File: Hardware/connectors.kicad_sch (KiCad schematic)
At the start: 0 parts

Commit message: Finalize schematic: Add connectors, LEDs, Buzzer and fix all ERC errors
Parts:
- added D1: D_Schottky, symbol Device:D_Schottky
- added J1: USB_C_Receptacle_USB2.0_16P, symbol Connector:USB_C_Receptacle_USB2.0_16P
- added J10: RX1, symbol Connector_Generic:Conn_01x01
- added J11: TX1, symbol Connector_Generic:Conn_01x01
- added J12, J16, J21, J25, J29, J3, J8: GND, symbol Connector_Generic:Conn_01x01
- added J13, J20, J22, J26, J30, J4, J6, J9: +5V, symbol Connector_Generic:Conn_01x01
- added J14: CAM_VIDEO_IN, symbol Connector_Generic:Conn_01x01
- added J15: +9V, symbol Connector_Generic:Conn_01x01
- added J17: VTX_VIDEO_OUT, symbol Connector_Generic:Conn_01x01
- added J18: TX3, symbol Connector_Generic:Conn_01x01
- added J19: RX3, symbol Connector_Generic:Conn_01x01
- added J2: Conn_01x08, symbol Connector_Generic:Conn_01x08
- added J23: RX2, symbol Connector_Generic:Conn_01x01
- added J24: TX2, symbol Connector_Generic:Conn_01x01
- added J27: RX5, symbol Connector_Generic:Conn_01x01
- added J28: TX5, symbol Connector_Generic:Conn_01x01
- added J31: RX6, symbol Connector_Generic:Conn_01x01
- added J32: TX6, symbol Connector_Generic:Conn_01x01
- added J5: LED_STRIP, symbol Connector_Generic:Conn_01x01
- added J7: BUZZER-, symbol Connector_Generic:Conn_01x01
- added R10, R9: 5.1k, symbol Device:R
- added R15: 330Ω, symbol Device:R
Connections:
- new net: D1.2 (A), J1.A4 (VBUS), J1.A9 (VBUS), J1.B4 (VBUS), J1.B9 (VBUS)
- new net: J1.A5 (CC1), R9.1
- new net: J1.B5 (CC2), R10.1
- new net: J5.1 (Pin_1), R15.2
- new net +5V: D1.1 (K), J13.1 (Pin_1), J20.1 (Pin_1), J22.1 (Pin_1), J26.1 (Pin_1), J30.1 (Pin_1), J4.1 (Pin_1), J6.1 (Pin_1), J9.1 (Pin_1)
- new net +9V: J15.1 (Pin_1)
- new net BAT+: J2.2 (Pin_2)
- new net BUZZER-: J7.1 (Pin_1)
- new net CAM_VIDEO_IN: J14.1 (Pin_1)
- new net CURRENT_SENSE: J2.7 (Pin_7)
- new net GND: J1.A1 (GND), J1.A12 (GND), J1.B1 (GND), J1.B12 (GND), J1.S1 (SHIELD), J12.1 (Pin_1), J16.1 (Pin_1), J2.1 (Pin_1), J21.1 (Pin_1), J25.1 (Pin_1), J29.1 (Pin_1), J3.1 (Pin_1), J8.1 (Pin_1), R10.2, R9.2
- new net LED_STRIP: R15.1
- new net MOTOR_1: J2.3 (Pin_3)
- new net MOTOR_2: J2.4 (Pin_4)
- new net MOTOR_3: J2.5 (Pin_5)
- new net MOTOR_4: J2.6 (Pin_6)
- new net RX1: J10.1 (Pin_1)
- new net RX2: J23.1 (Pin_1)
- new net RX3: J19.1 (Pin_1)
- new net RX4: J2.8 (Pin_8)
- new net RX5: J27.1 (Pin_1)
- new net RX6: J31.1 (Pin_1)
- new net TX1: J11.1 (Pin_1)
- new net TX2: J24.1 (Pin_1)
- new net TX3: J18.1 (Pin_1)
- new net TX5: J28.1 (Pin_1)
- new net TX6: J32.1 (Pin_1)
- new net USB_DM: J1.A7 (D-), J1.B7 (D-)
- new net USB_DP: J1.A6 (D+), J1.B6 (D+)
- new net VTX_VIDEO_OUT: J17.1 (Pin_1)
- no-connect marks 0 -> 2
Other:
- note added: "Buzzer"
- note added: "CAMERA"
- note added: "ESC & POWER"
- note added: "LED STRIP"
- note added: "UART 1"
- note added: "UART 2"
- note added: "UART 5"
- note added: "UART 6"
- note added: "USB INTERFACE"
- note added: "VIDEO SYSTEM"
- note added: "VTX"

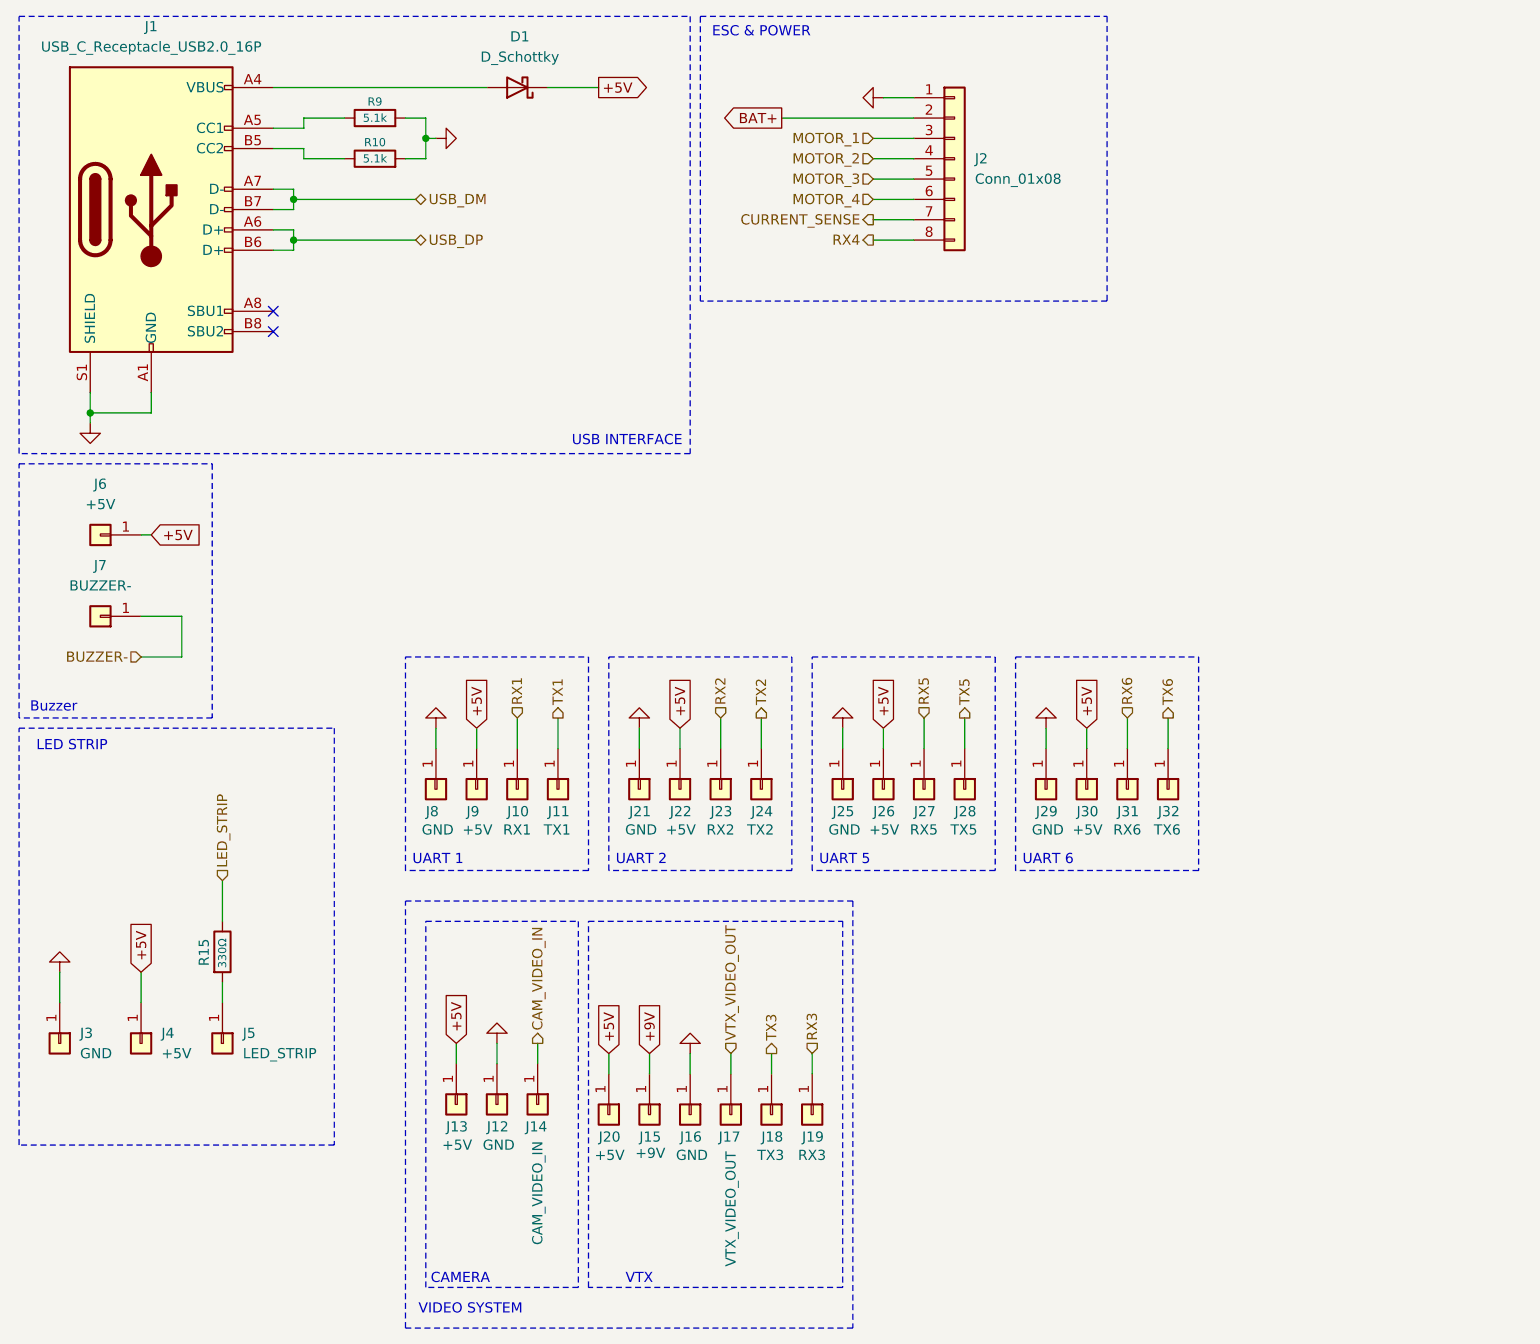
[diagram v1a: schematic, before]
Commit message: Update schematic: Add SDIO Blackbox, ESC Redundancy and remove UART5
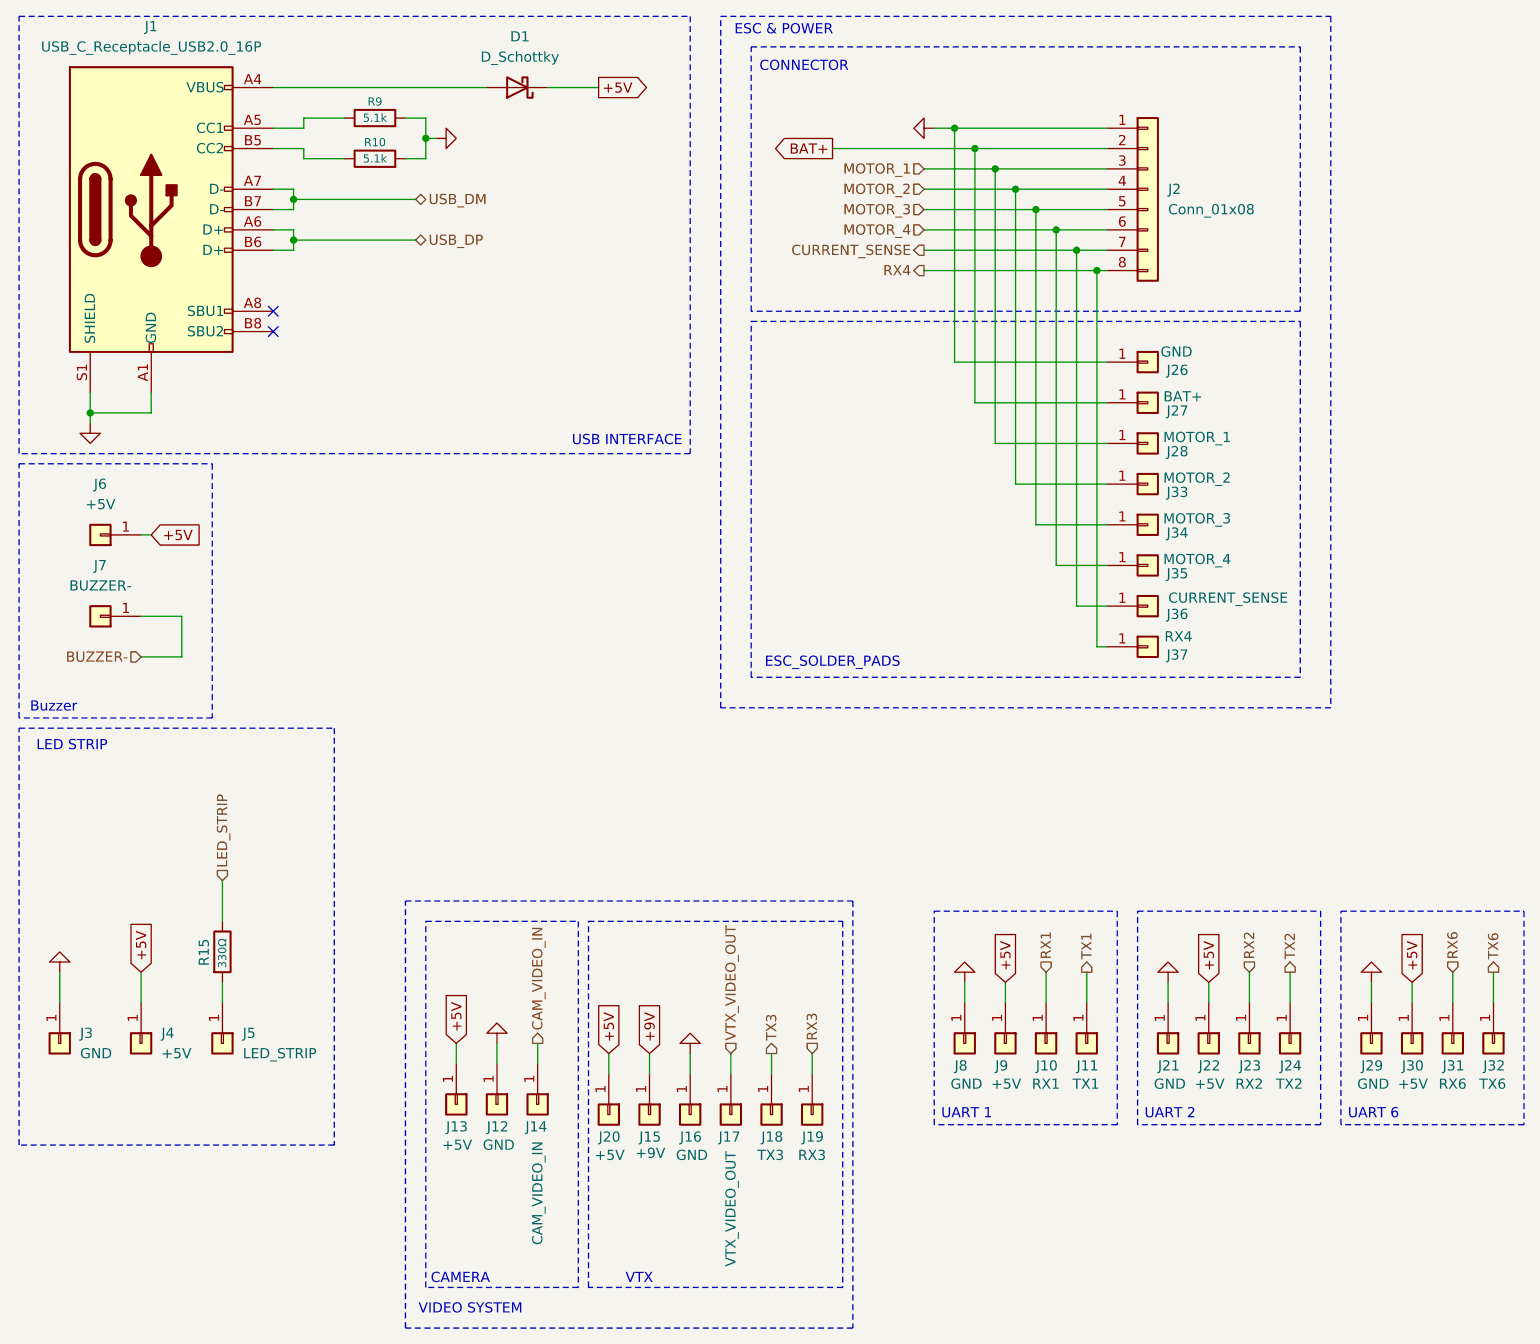
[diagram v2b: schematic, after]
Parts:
- removed J25: GND, symbol Connector_Generic:Conn_01x01
- added J33: MOTOR_2, symbol Connector_Generic:Conn_01x01
- added J34: MOTOR_3, symbol Connector_Generic:Conn_01x01
- added J35: MOTOR_4, symbol Connector_Generic:Conn_01x01
- added J36: CURRENT_SENSE, symbol Connector_Generic:Conn_01x01
- added J37: RX4, symbol Connector_Generic:Conn_01x01
- J26: value +5V -> GND
- J27: value RX5 -> BAT+
- J28: value TX5 -> MOTOR_1
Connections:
- net RX5 is gone; now on net BAT+: J27.1 (Pin_1)
- net TX5 is gone; now on net MOTOR_1: J28.1 (Pin_1)
- net +5V: no longer J26.1 (Pin_1)
- net CURRENT_SENSE: now also J36.1 (Pin_1)
- net GND: now also J26.1 (Pin_1)
- net MOTOR_2: now also J33.1 (Pin_1)
- net MOTOR_3: now also J34.1 (Pin_1)
- net MOTOR_4: now also J35.1 (Pin_1)
- net RX4: now also J37.1 (Pin_1)
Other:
- note added: "CONNECTOR"
- note added: "ESC_SOLDER_PADS"
- note removed: "UART 5"
- moved on the sheet: J10, J11, J2, J21, J22, J23, J24, J29, J30, J31, J32, J8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

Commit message: Finalize component placement and silkscreen
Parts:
- D1: footprint (none) -> Diode_SMD:D_SOD-323
- J1: footprint (none) -> Connector_USB:USB_C_Receptacle_GCT_USB4085
- J10, J11, J12, J13, J14, J15, J16, J17, J18, J19, J20, J21, J22, J23, J24, J26, J27, J28, J29, J3, J30, J31, J32, J33, J34, J35, J36, J37, J4, J5, J6, J7, J8, J9: footprint (none) -> TestPoint:TestPoint_Pad_D1.5mm
- J2: footprint (none) -> Connector_JST:JST_SH_SM08B-SRSS-TB_1x08-1MP_P1.00mm_Horizontal
- R10, R15, R9: footprint (none) -> Resistor_SMD:R_0402_1005Metric
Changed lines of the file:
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@@
 			)
 		)
-		(property "Footprint" ""
+		(property "Footprint" "Connector_JST:JST_SH_SM08B-SRSS-TB_1x08-1MP_P1.00mm_Horizontal"
 			(at 153.67 34.29 0)
 			(effects
@@
 			)
 		)
-		(property "Footprint" ""
+		(property "Footprint" "TestPoint:TestPoint_Pad_D1.5mm"
 			(at 27.94 140.97 0)
 			(effects
@@
 			)
 		)
-		(property "Footprint" ""
+		(property "Footprint" "TestPoint:TestPoint_Pad_D1.5mm"
 			(at 130.81 140.97 0)
 			(effects
@@
 			)
 		)
-		(property "Footprint" ""
+		(property "Footprint" "TestPoint:TestPoint_Pad_D1.5mm"
 			(at 171.45 140.97 0)
 			(effects
@@
 			)
 		)
-		(property "Footprint" ""
+		(property "Footprint" "TestPoint:TestPoint_Pad_D1.5mm"
 			(at 106.68 149.86 0)
 			(effects
@@
 			)
 		)
-		(property "Footprint" ""
+		(property "Footprint" "TestPoint:TestPoint_Pad_D1.5mm"
 			(at 153.67 76.2 0)
 			(effects
@@
 			)
 		)
-		(property "Footprint" ""
+		(property "Footprint" "Diode_SMD:D_SOD-323"
 			(at 74.93 21.59 0)
 			(effects
@@
 			)
 		)
-		(property "Footprint" ""
+		(property "Footprint" "TestPoint:TestPoint_Pad_D1.5mm"
 			(at 67.31 148.59 0)
 			(effects
@@
 			)
 		)
-		(property "Footprint" ""
+		(property "Footprint" "TestPoint:TestPoint_Pad_D1.5mm"
 			(at 153.67 81.28 0)
 			(effects
@@
 			)
 		)
-		(property "Footprint" ""
+		(property "Footprint" "TestPoint:TestPoint_Pad_D1.5mm"
 			(at 17.78 140.97 0)
 			(effects
@@
 			)
 		)
-		(property "Footprint" ""
+		(property "Footprint" "TestPoint:TestPoint_Pad_D1.5mm"
 			(at 96.52 149.86 0)
 			(effects
@@
 			)
 		)
-		(property "Footprint" ""
+		(property "Footprint" "TestPoint:TestPoint_Pad_D1.5mm"
 			(at 166.37 140.97 0)
 			(effects
@@
 			)
 		)
-		(property "Footprint" ""
+		(property "Footprint" "Resistor_SMD:R_0402_1005Metric"
 			(at 57.15 27.178 90)
 			(effects
@@
 			)
 		)
-		(property "Footprint" ""
+		(property "Footprint" "TestPoint:TestPoint_Pad_D1.5mm"
 			(at 153.67 55.88 0)
 			(effects
@@
 			)
 		)
-		(property "Footprint" ""
+		(property "Footprint" "TestPoint:TestPoint_Pad_D1.5mm"
 			(at 86.36 149.86 0)
 			(effects
@@
 			)
 		)
-		(property "Footprint" ""
+		(property "Footprint" "TestPoint:TestPoint_Pad_D1.5mm"
 			(at 161.29 140.97 0)
 			(effects
@@
 			)
 		)
-		(property "Footprint" ""
+		(property "Footprint" "Resistor_SMD:R_0402_1005Metric"
 			(at 57.15 32.258 90)
 			(effects
@@
 			)
 		)
-		(property "Footprint" ""
+		(property "Footprint" "TestPoint:TestPoint_Pad_D1.5mm"
 			(at 181.61 140.97 0)
 			(effects
@@
 			)
 		)
-		(property "Footprint" ""
+		(property "Footprint" "TestPoint:TestPoint_Pad_D1.5mm"
 			(at 77.47 148.59 0)
 			(effects
@@
 			)
 		)
-		(property "Footprint" ""
+		(property "Footprint" "Resistor_SMD:R_0402_1005Metric"
 			(at 36.322 129.54 90)
 			(effects
@@
 			)
 		)
-		(property "Footprint" ""
+		(property "Footprint" "TestPoint:TestPoint_Pad_D1.5mm"
 			(at 22.86 77.47 0)
 			(effects
@@
 			)
 		)
-		(property "Footprint" ""
+		(property "Footprint" "TestPoint:TestPoint_Pad_D1.5mm"
 			(at 101.6 149.86 0)
 			(effects
@@
 			)
 		)
-		(property "Footprint" ""
+		(property "Footprint" "TestPoint:TestPoint_Pad_D1.5mm"
 			(at 135.89 140.97 0)
 			(effects
@@
 			)
 		)
-		(property "Footprint" ""
+		(property "Footprint" "TestPoint:TestPoint_Pad_D1.5mm"
 			(at 22.86 87.63 0)
 			(effects
@@
 			)
 		)
-		(property "Footprint" ""
+		(property "Footprint" "TestPoint:TestPoint_Pad_D1.5mm"
 			(at 153.67 86.36 0)
 			(effects
@@
 			)
 		)
-		(property "Footprint" ""
+		(property "Footprint" "TestPoint:TestPoint_Pad_D1.5mm"
 			(at 156.21 140.97 0)
 			(effects
@@
 			)
 		)
-		(property "Footprint" ""
+		(property "Footprint" "TestPoint:TestPoint_Pad_D1.5mm"
 			(at 196.85 140.97 0)
 			(effects
@@
 			)
 		)
-		(property "Footprint" ""
+		(property "Footprint" "TestPoint:TestPoint_Pad_D1.5mm"
 			(at 153.67 71.12 0)
 			(effects
@@
 			)
 		)
-		(property "Footprint" ""
+		(property "Footprint" "TestPoint:TestPoint_Pad_D1.5mm"
 			(at 153.67 91.44 0)
 			(effects
@@
 			)
 		)
-		(property "Footprint" ""
+		(property "Footprint" "TestPoint:TestPoint_Pad_D1.5mm"
 			(at 91.44 149.86 0)
 			(effects
@@
 			)
 		)
-		(property "Footprint" ""
+		(property "Footprint" "TestPoint:TestPoint_Pad_D1.5mm"
 			(at 153.67 66.04 0)
 			(effects
@@
 			)
 		)
-		(property "Footprint" ""
+		(property "Footprint" "Connector_USB:USB_C_Receptacle_GCT_USB4085"
 			(at 33.02 36.83 0)
 			(effects
@@
 			)
 		)
-		(property "Footprint" ""
+		(property "Footprint" "TestPoint:TestPoint_Pad_D1.5mm"
 			(at 186.69 140.97 0)
 			(effects
@@
 			)
 		)
-		(property "Footprint" ""
+		(property "Footprint" "TestPoint:TestPoint_Pad_D1.5mm"
 			(at 38.1 140.97 0)
 			(effects
@@
 			)
 		)
-		(property "Footprint" ""
+		(property "Footprint" "TestPoint:TestPoint_Pad_D1.5mm"
 			(at 146.05 140.97 0)
 			(effects
@@
 			)
 		)
-		(property "Footprint" ""
+		(property "Footprint" "TestPoint:TestPoint_Pad_D1.5mm"
 			(at 72.39 148.59 0)
 			(effects
@@
 			)
 		)
-		(property "Footprint" ""
+		(property "Footprint" "TestPoint:TestPoint_Pad_D1.5mm"
 			(at 111.76 149.86 0)
 			(effects
@@
 			)
 		)
-		(property "Footprint" ""
+		(property "Footprint" "TestPoint:TestPoint_Pad_D1.5mm"
 			(at 140.97 140.97 0)
 			(effects
@@
 			)
 		)
-		(property "Footprint" ""
+		(property "Footprint" "TestPoint:TestPoint_Pad_D1.5mm"
 			(at 191.77 140.97 0)
 			(effects
@@
 			)
 		)
-		(property "Footprint" ""
+		(property "Footprint" "TestPoint:TestPoint_Pad_D1.5mm"
 			(at 153.67 60.96 0)
 			(effects
